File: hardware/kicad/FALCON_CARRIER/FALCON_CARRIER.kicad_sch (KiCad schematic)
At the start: 0 parts

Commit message: Add FALCON carrier schematic v0.1
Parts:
- added J1: POWER_INPUT, symbol FALCON:POWER_INPUT
- added J10: LEAK_SENSOR_TBD, symbol FALCON:LEAK_SENSOR_TBD
- added J11: FAN_TBD, symbol FALCON:FAN_TBD
- added J12: SERVICE_I2C, symbol FALCON:SERVICE_I2C
- added J2: BAR02_I2C, symbol FALCON:BAR02_I2C
- added J3: GPS_UART, symbol FALCON:GPS_UART
- added J4: INA260_BAT_LOGIC, symbol FALCON:INA260_BAT_LOGIC
- added J5: INA260_SOLAR_0X41, symbol FALCON:INA260_SOLAR_0X41
- added J6: MCP9808_0X18, symbol FALCON:MCP9808_0X18
- added J7: ANEMOMETER, symbol FALCON:ANEMOMETER
- added J8: WIND_VANE, symbol FALCON:WIND_VANE
- added J9: DS18B20_OPTION, symbol FALCON:DS18B20_OPTION
- added R1: PULLUP_10K, symbol FALCON:PULLUP_10K
- added R2: PULLUP_4K7, symbol FALCON:PULLUP_4K7
- added U1: REGULATOR_3V3_TBD, symbol FALCON:REGULATOR_3V3_TBD
- added U2: ESP32_DEVKIT_INTERFACE, symbol FALCON:ESP32_DEVKIT_INTERFACE
- added U3: BNO085_SPI, symbol FALCON:BNO085_SPI
- added U4: ADS1115_0X48, symbol FALCON:ADS1115_0X48
- added U5: FAN_DRIVER_TBD, symbol FALCON:FAN_DRIVER_TBD
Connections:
- new net +3V3_SENSOR: J10.1 (+3V3_SENSOR), J12.1 (+3V3_SENSOR), J2.1 (+3V3_SENSOR), J3.1 (+3V3_SENSOR), J4.1 (+3V3_SENSOR), J5.1 (+3V3_SENSOR), J6.1 (+3V3_SENSOR), J7.1 (+3V3_SENSOR), J8.1 (+3V3_SENSOR), J9.1 (+3V3_SENSOR), R1.1 (+3V3_SENSOR), R2.1 (+3V3_SENSOR), U1.3 (+3V3_SENSOR), U2.2 (+3V3_SENSOR), U3.1 (+3V3_SENSOR), U3.10 (+3V3_SENSOR), U3.9 (+3V3_SENSOR), U4.1 (+3V3_SENSOR)
- new net +5V_PROTECTED: J1.1 (+5V_PROTECTED), J11.1 (+5V_PROTECTED), U1.1 (+5V_PROTECTED), U2.1 (+5V_PROTECTED), U5.1 (+5V_PROTECTED)
- new net BNO_CS: U2.9 (BNO_CS), U3.6 (BNO_CS)
- new net BNO_INT: U2.10 (BNO_INT), U3.7 (BNO_INT)
- new net BNO_MISO: U2.7 (BNO_MISO), U3.4 (BNO_MISO)
- new net BNO_MOSI: U2.8 (BNO_MOSI), U3.5 (BNO_MOSI)
- new net BNO_RST: U2.11 (BNO_RST), U3.8 (BNO_RST)
- new net BNO_SCK: U2.6 (BNO_SCK), U3.3 (BNO_SCK)
- new net FAN_PWM: U2.17 (FAN_PWM), U5.3 (FAN_PWM)
- new net FAN_SWITCHED: J11.2 (FAN_SWITCHED), U5.4 (FAN_SWITCHED)
- new net GND: J1.2 (GND), J10.3 (GND), J12.2 (GND), J2.2 (GND), J3.2 (GND), J4.2 (GND), J5.2 (GND), J6.2 (GND), J7.3 (GND), J8.3 (GND), J9.3 (GND), U1.2 (GND), U2.3 (GND), U3.2 (GND), U4.2 (GND), U5.2 (GND)
- new net GPS_RX: J3.4 (GPS_RX), U2.13 (GPS_RX)
- new net GPS_TX: J3.3 (GPS_TX), U2.12 (GPS_TX)
- new net I2C_SCL: J12.3 (I2C_SCL), J2.3 (I2C_SCL), J4.3 (I2C_SCL), J5.3 (I2C_SCL), J6.3 (I2C_SCL), U2.5 (I2C_SCL), U4.3 (I2C_SCL)
- new net I2C_SDA: J12.4 (I2C_SDA), J2.4 (I2C_SDA), J4.4 (I2C_SDA), J5.4 (I2C_SDA), J6.4 (I2C_SDA), U2.4 (I2C_SDA), U4.4 (I2C_SDA)
- new net LEAK_SIGNAL: J10.2 (LEAK_SIGNAL), U2.16 (LEAK_SIGNAL)
- new net WATER_TEMP: J9.2 (WATER_TEMP), R2.2 (WATER_TEMP), U2.15 (WATER_TEMP)
- new net WIND_PULSE: J7.2 (WIND_PULSE), R1.2 (WIND_PULSE), U2.14 (WIND_PULSE)
- new net WIND_VANE: J8.2 (WIND_VANE), U4.5 (WIND_VANE)

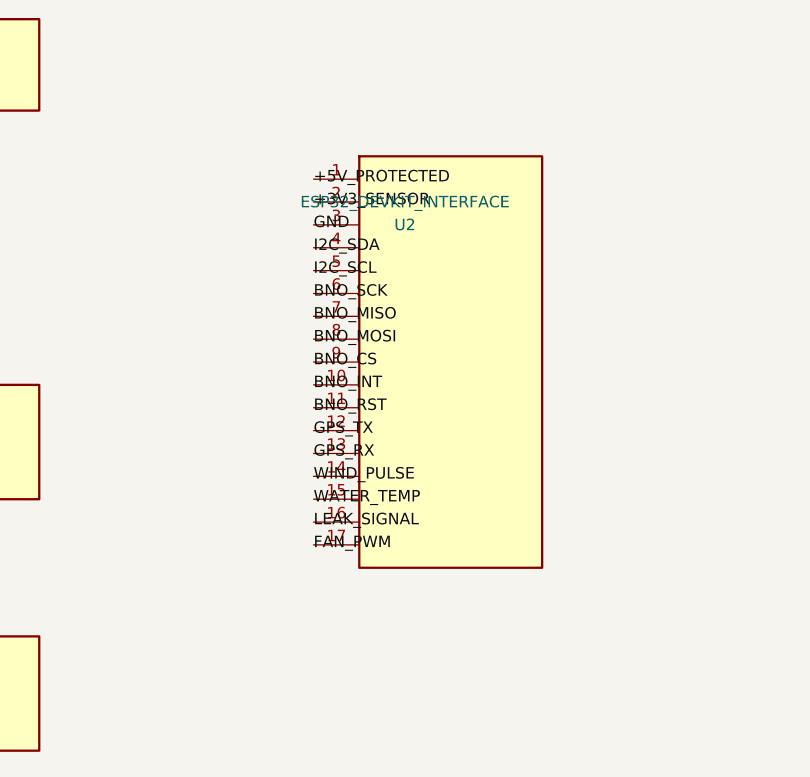
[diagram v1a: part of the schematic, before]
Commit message: Lock carrier PCB to official ESP32-DevKitC V4
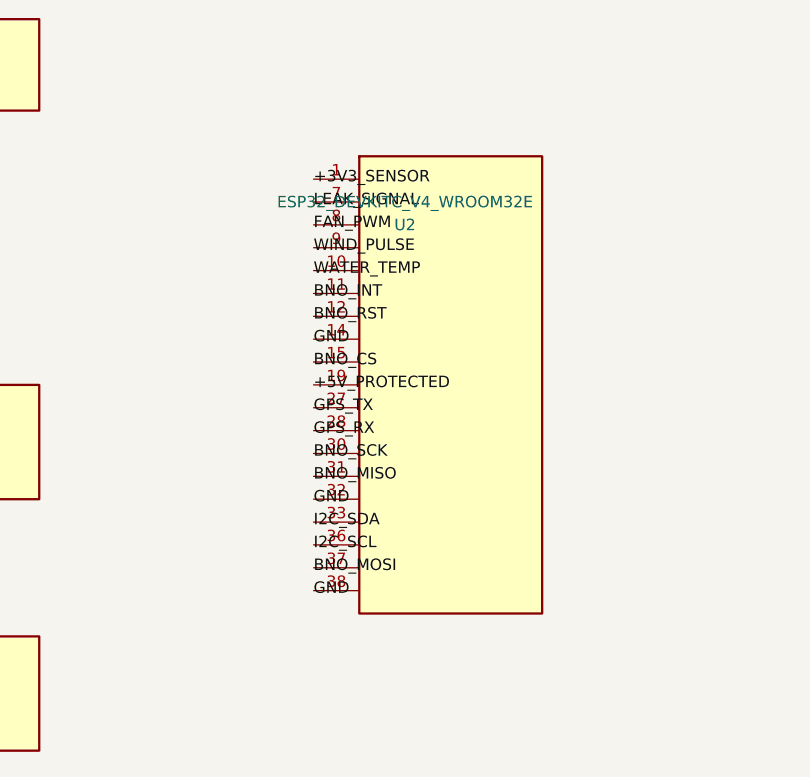
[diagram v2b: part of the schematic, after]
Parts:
- U2: value ESP32_DEVKIT_INTERFACE -> ESP32_DEVKITC_V4_WROOM32E; symbol FALCON:ESP32_DEVKIT_INTERFACE -> FALCON:ESP32_DEVKITC_V4_WROOM32E
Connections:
- net +3V3_SENSOR: now also U2.1 (+3V3_SENSOR); no longer U2.2 (+3V3_SENSOR)
- net +5V_PROTECTED: now also U2.19 (+5V_PROTECTED); no longer U2.1 (+5V_PROTECTED)
- net BNO_CS: now also U2.15 (BNO_CS); no longer U2.9 (BNO_CS)
- net BNO_INT: now also U2.11 (BNO_INT); no longer U2.10 (BNO_INT)
- net BNO_MISO: now also U2.31 (BNO_MISO); no longer U2.7 (BNO_MISO)
- net BNO_MOSI: now also U2.37 (BNO_MOSI); no longer U2.8 (BNO_MOSI)
- net BNO_RST: now also U2.12 (BNO_RST); no longer U2.11 (BNO_RST)
- net BNO_SCK: now also U2.30 (BNO_SCK); no longer U2.6 (BNO_SCK)
- net FAN_PWM: now also U2.8 (FAN_PWM); no longer U2.17 (FAN_PWM)
- net GND: now also U2.14 (GND), U2.32 (GND), U2.38 (GND); no longer U2.3 (GND)
- net GPS_RX: now also U2.28 (GPS_RX); no longer U2.13 (GPS_RX)
- net GPS_TX: now also U2.27 (GPS_TX); no longer U2.12 (GPS_TX)
- net I2C_SCL: now also U2.36 (I2C_SCL); no longer U2.5 (I2C_SCL)
- net I2C_SDA: now also U2.33 (I2C_SDA); no longer U2.4 (I2C_SDA)
- net LEAK_SIGNAL: now also U2.7 (LEAK_SIGNAL); no longer U2.16 (LEAK_SIGNAL)
- net WATER_TEMP: now also U2.10 (WATER_TEMP); no longer U2.15 (WATER_TEMP)
- net WIND_PULSE: now also U2.9 (WIND_PULSE); no longer U2.14 (WIND_PULSE)
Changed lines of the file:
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@@
   (label "+3V3_SENSOR" (at 88.90 40.64 0)
     (effects (font (size 1.27 1.27))))
-  (label "+5V_PROTECTED" (at 144.78 50.80 0)
-    (effects (font (size 1.27 1.27))))
-  (label "+3V3_SENSOR" (at 144.78 53.34 0)
-    (effects (font (size 1.27 1.27))))
-  (label "GND" (at 144.78 55.88 0)
-    (effects (font (size 1.27 1.27))))
-  (label "I2C_SDA" (at 144.78 58.42 0)
-    (effects (font (size 1.27 1.27))))
-  (label "I2C_SCL" (at 144.78 60.96 0)
-    (effects (font (size 1.27 1.27))))
-  (label "BNO_SCK" (at 144.78 63.50 0)
-    (effects (font (size 1.27 1.27))))
-  (label "BNO_MISO" (at 144.78 66.04 0)
-    (effects (font (size 1.27 1.27))))
-  (label "BNO_MOSI" (at 144.78 68.58 0)
+  (label "+3V3_SENSOR" (at 144.78 50.80 0)
+    (effects (font (size 1.27 1.27))))
+  (label "LEAK_SIGNAL" (at 144.78 53.34 0)
+    (effects (font (size 1.27 1.27))))
+  (label "FAN_PWM" (at 144.78 55.88 0)
+    (effects (font (size 1.27 1.27))))
+  (label "WIND_PULSE" (at 144.78 58.42 0)
+    (effects (font (size 1.27 1.27))))
+  (label "WATER_TEMP" (at 144.78 60.96 0)
+    (effects (font (size 1.27 1.27))))
+  (label "BNO_INT" (at 144.78 63.50 0)
+    (effects (font (size 1.27 1.27))))
+  (label "BNO_RST" (at 144.78 66.04 0)
+    (effects (font (size 1.27 1.27))))
+  (label "GND" (at 144.78 68.58 0)
     (effects (font (size 1.27 1.27))))
   (label "BNO_CS" (at 144.78 71.12 0)
     (effects (font (size 1.27 1.27))))
-  (label "BNO_INT" (at 144.78 73.66 0)
-    (effects (font (size 1.27 1.27))))
-  (label "BNO_RST" (at 144.78 76.20 0)
-    (effects (font (size 1.27 1.27))))
-  (label "GPS_TX" (at 144.78 78.74 0)
-    (effects (font (size 1.27 1.27))))
-  (label "GPS_RX" (at 144.78 81.28 0)
-    (effects (font (size 1.27 1.27))))
-  (label "WIND_PULSE" (at 144.78 83.82 0)
-    (effects (font (size 1.27 1.27))))
-  (label "WATER_TEMP" (at 144.78 86.36 0)
-    (effects (font (size 1.27 1.27))))
-  (label "LEAK_SIGNAL" (at 144.78 88.90 0)
-    (effects (font (size 1.27 1.27))))
-  (label "FAN_PWM" (at 144.78 91.44 0)
+  (label "+5V_PROTECTED" (at 144.78 73.66 0)
+    (effects (font (size 1.27 1.27))))
+  (label "GPS_TX" (at 144.78 76.20 0)
+    (effects (font (size 1.27 1.27))))
+  (label "GPS_RX" (at 144.78 78.74 0)
+    (effects (font (size 1.27 1.27))))
+  (label "BNO_SCK" (at 144.78 81.28 0)
+    (effects (font (size 1.27 1.27))))
+  (label "BNO_MISO" (at 144.78 83.82 0)
+    (effects (font (size 1.27 1.27))))
+  (label "GND" (at 144.78 86.36 0)
+    (effects (font (size 1.27 1.27))))
+  (label "I2C_SDA" (at 144.78 88.90 0)
+    (effects (font (size 1.27 1.27))))
+  (label "I2C_SCL" (at 144.78 91.44 0)
+    (effects (font (size 1.27 1.27))))
+  (label "BNO_MOSI" (at 144.78 93.98 0)
+    (effects (font (size 1.27 1.27))))
+  (label "GND" (at 144.78 96.52 0)
     (effects (font (size 1.27 1.27))))
   (label "+3V3_SENSOR" (at 210.82 45.72 0)
@@
   )
   (symbol
-    (lib_id "FALCON:ESP32_DEVKIT_INTERFACE") (at 154.94 50.80 0) (unit 1)
+    (lib_id "FALCON:ESP32_DEVKITC_V4_WROOM32E") (at 154.94 50.80 0) (unit 1)
     (exclude_from_sim no) (in_bom yes) (on_board yes) (dnp no)
     (property "Reference" "U2" (at 154.94 55.88 0) (effects (font (size 1.27 1.27))))
-    (property "Value" "ESP32_DEVKIT_INTERFACE" (at 154.94 53.34 0) (effects (font (size 1.27 1.27))))
+    (property "Value" "ESP32_DEVKITC_V4_WROOM32E" (at 154.94 53.34 0) (effects (font (size 1.27 1.27))))
     (property "Footprint" "" (at 154.94 50.80 0) (effects (font (size 1.27 1.27)) (hide yes)))
     (property "Datasheet" "" (at 154.94 50.80 0) (effects (font (size 1.27 1.27)) (hide yes)))
     (property "Description" "FALCON carrier placeholder; footprint TBD" (at 154.94 50.80 0) (effects (font (size 1.27 1.27)) (hide yes)))
     (pin "1")
-    (pin "2")
-    (pin "3")
-    (pin "4")
-    (pin "5")
-    (pin "6")
     (pin "7")
     (pin "8")
@@
     (pin "11")
     (pin "12")
-    (pin "13")
     (pin "14")
     (pin "15")
-    (pin "16")
-    (pin "17")
+    (pin "19")
+    (pin "27")
+    (pin "28")
+    (pin "30")
+    (pin "31")
+    (pin "32")
+    (pin "33")
+    (pin "36")
+    (pin "37")
+    (pin "38")
     (instances (project "FALCON_CARRIER"
       (path "/8f84bda8-4a60-4fb6-9df1-43d0356dc759" (reference "U2") (unit 1))))

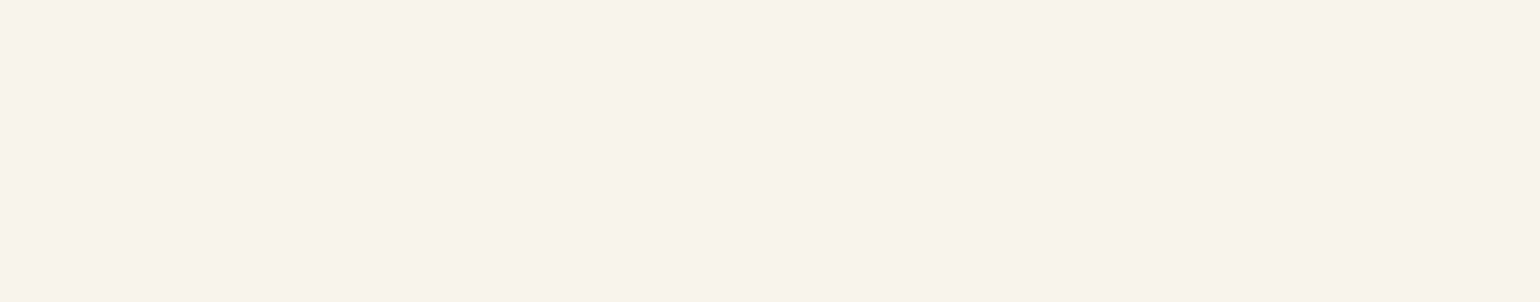
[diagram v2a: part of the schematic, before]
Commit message: Add carrier PCB service test points
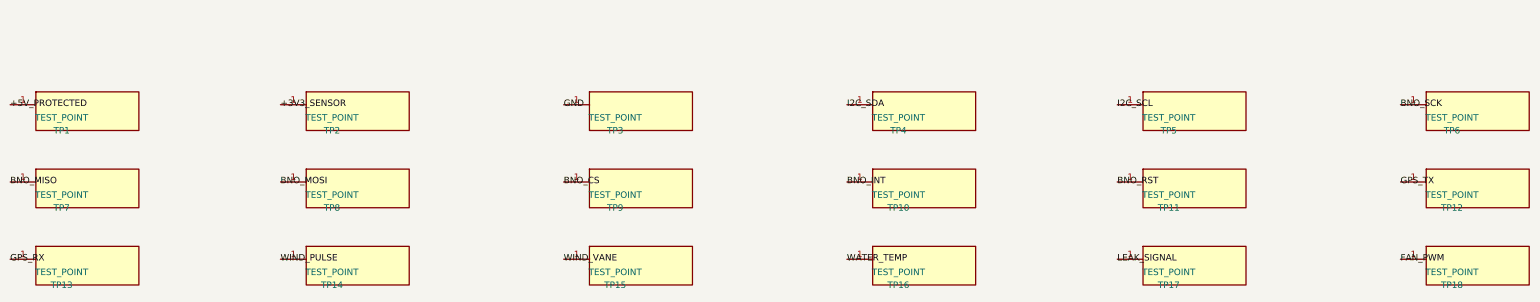
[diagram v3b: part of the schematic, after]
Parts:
- added TP1, TP10, TP11, TP12, TP13, TP14, TP15, TP16, TP17, TP18, TP2, TP3, TP4, TP5, TP6, TP7, TP8, TP9: TEST_POINT, symbol FALCON:TEST_POINT
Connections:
- net +3V3_SENSOR: now also TP2.1 (+5V_PROTECTED)
- net +5V_PROTECTED: now also TP1.1 (+5V_PROTECTED)
- net BNO_CS: now also TP9.1 (+5V_PROTECTED)
- net BNO_INT: now also TP10.1 (+5V_PROTECTED)
- net BNO_MISO: now also TP7.1 (+5V_PROTECTED)
- net BNO_MOSI: now also TP8.1 (+5V_PROTECTED)
- net BNO_RST: now also TP11.1 (+5V_PROTECTED)
- net BNO_SCK: now also TP6.1 (+5V_PROTECTED)
- net FAN_PWM: now also TP18.1 (+5V_PROTECTED)
- net GND: now also TP3.1 (+5V_PROTECTED)
- net GPS_RX: now also TP13.1 (+5V_PROTECTED)
- net GPS_TX: now also TP12.1 (+5V_PROTECTED)
- net I2C_SCL: now also TP5.1 (+5V_PROTECTED)
- net I2C_SDA: now also TP4.1 (+5V_PROTECTED)
- net LEAK_SIGNAL: now also TP17.1 (+5V_PROTECTED)
- net WATER_TEMP: now also TP16.1 (+5V_PROTECTED)
- net WIND_PULSE: now also TP14.1 (+5V_PROTECTED)
- net WIND_VANE: now also TP15.1 (+5V_PROTECTED)

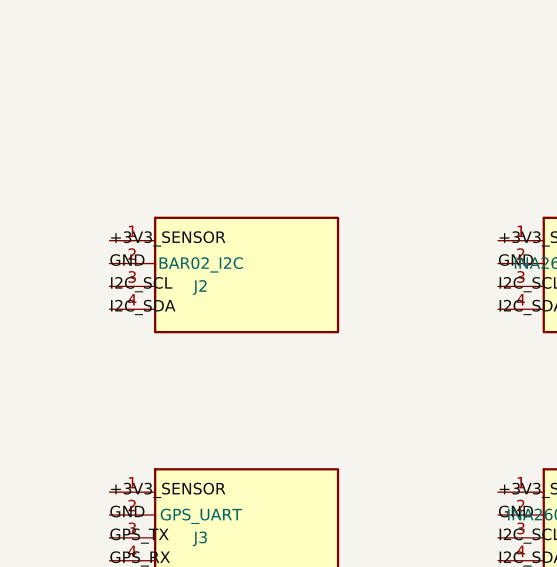
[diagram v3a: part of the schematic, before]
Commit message: Research carrier module dimensions and fix Bar02 pinout
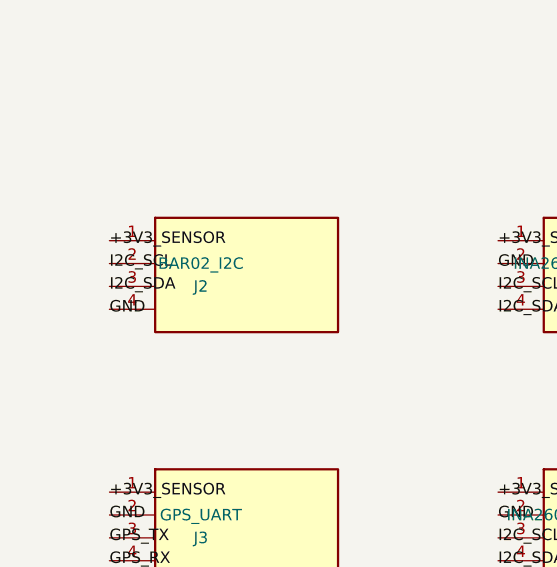
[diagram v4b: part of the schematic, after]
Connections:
- net GND: now also J2.4 (GND); no longer J2.2 (GND)
- net I2C_SCL: now also J2.2 (I2C_SCL); no longer J2.3 (I2C_SCL)
- net I2C_SDA: now also J2.3 (I2C_SDA); no longer J2.4 (I2C_SDA)
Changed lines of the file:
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@@
   (label "+3V3_SENSOR" (at 45.72 76.20 0)
     (effects (font (size 1.27 1.27))))
-  (label "GND" (at 45.72 78.74 0)
+  (label "I2C_SCL" (at 45.72 78.74 0)
     (effects (font (size 1.27 1.27))))
-  (label "I2C_SCL" (at 45.72 81.28 0)
+  (label "I2C_SDA" (at 45.72 81.28 0)
     (effects (font (size 1.27 1.27))))
-  (label "I2C_SDA" (at 45.72 83.82 0)
+  (label "GND" (at 45.72 83.82 0)
     (effects (font (size 1.27 1.27))))
   (label "+3V3_SENSOR" (at 45.72 104.14 0)
